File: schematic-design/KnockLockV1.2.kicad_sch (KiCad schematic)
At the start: 39 parts, among them IC1 ESP32-C3-WROOM-02-N4, IC2 LM2575-3.3WT, IC3 MC74HC74ADTR2G, J1 2477, J2 UJ20-C-H-G-TH-P16-TR, J3 TBP04R12-500-03BE, Q1 IRLML6402TRPBF, Q2 BC547B, U1 ADXL345BCCZ-RL7

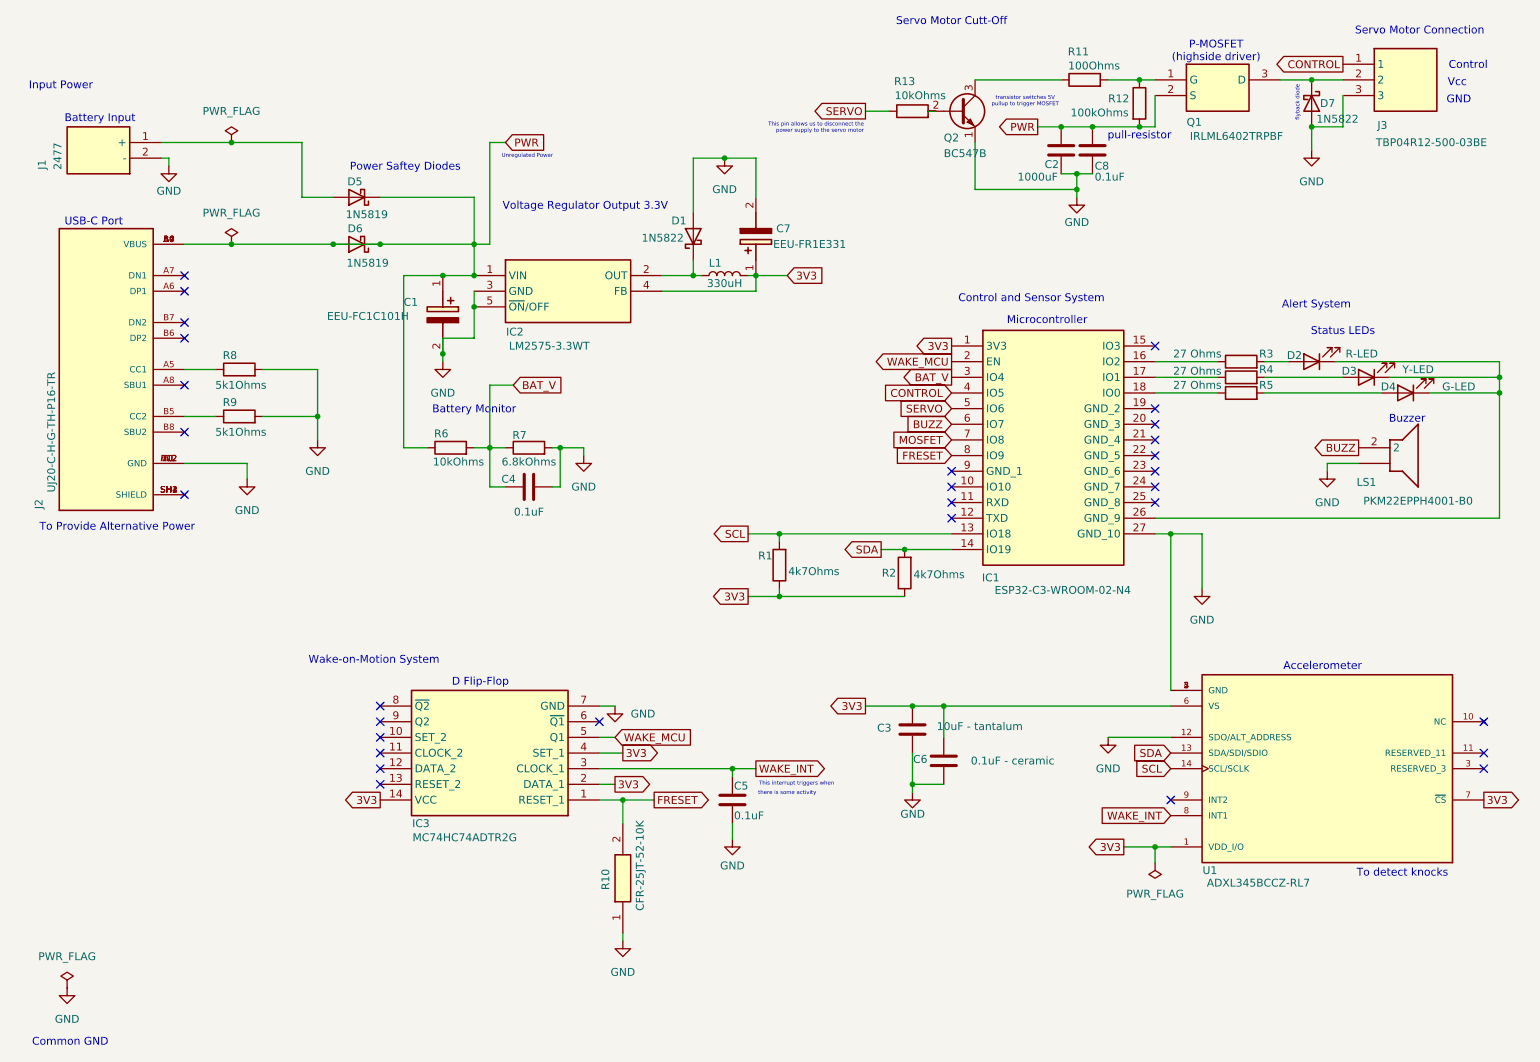
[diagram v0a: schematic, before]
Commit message: Fixed power gating
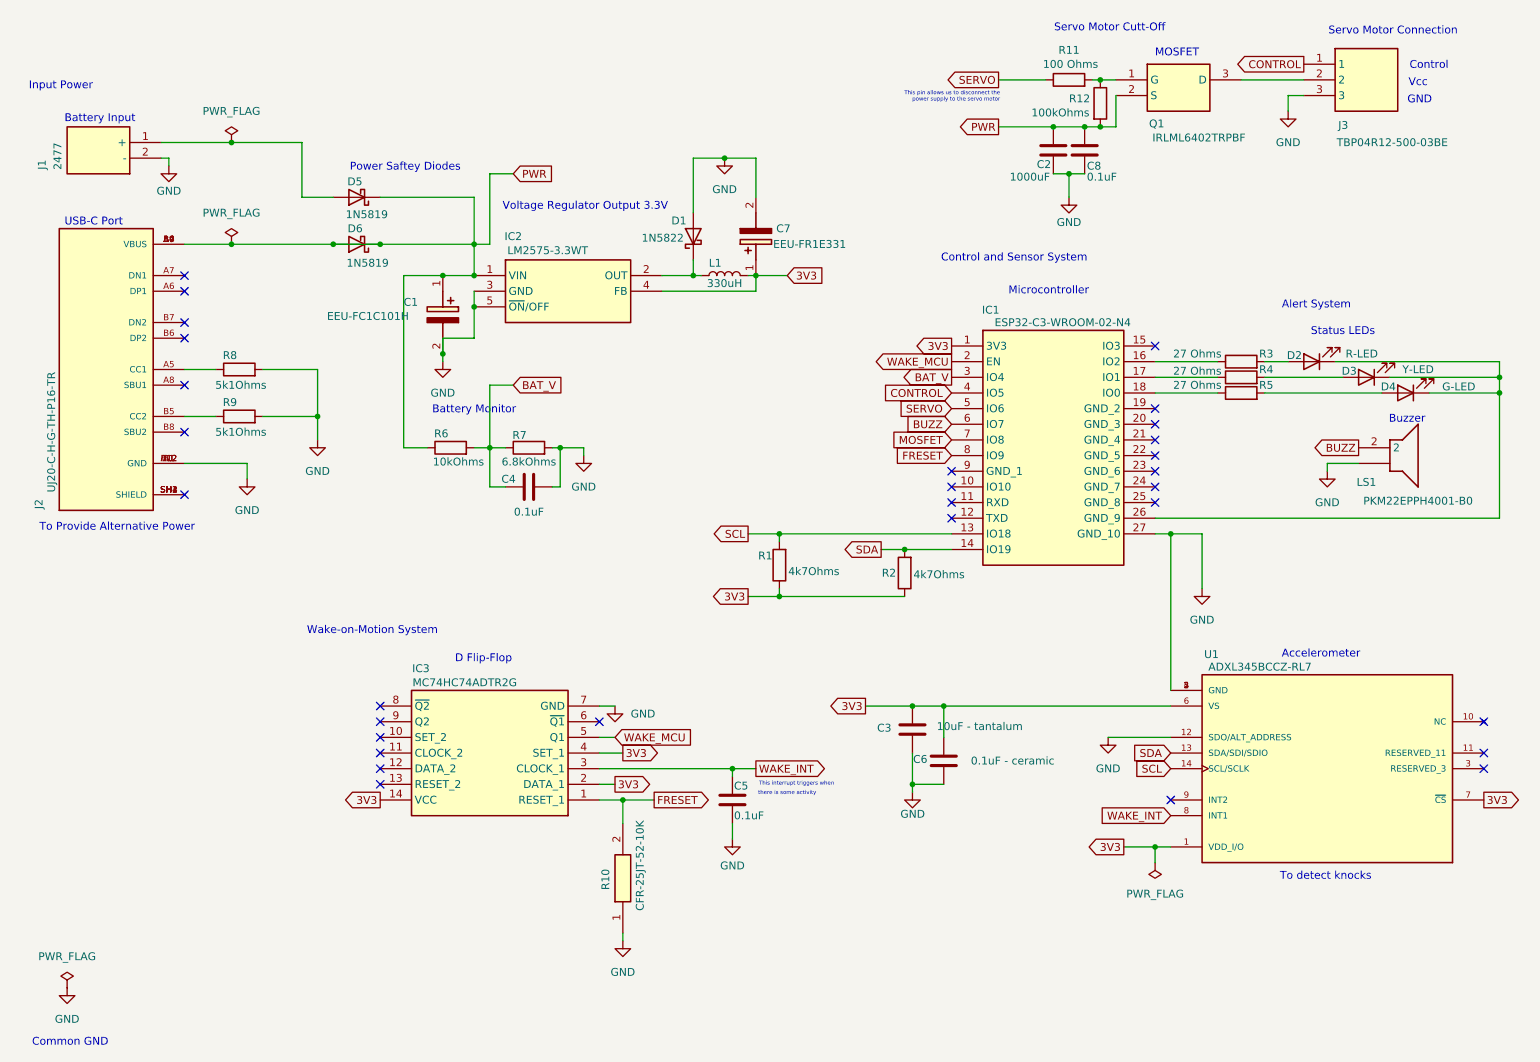
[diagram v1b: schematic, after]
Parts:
- removed D7: 1N5822, Diode_THT:D_DO-201AD_P15.24mm_Horizontal, symbol Diode:1N5822
- removed Q2: BC547B, Package_TO_SOT_THT:TO-92_HandSolder, symbol Transistor_BJT:2N3904
- removed R13: 10kOhms, symbol Device:R
- R11: value 100Ohms -> 100 Ohms
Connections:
- net SERVO: now also R11.1
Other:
- note added: "MOSFET"
- note removed: "P-MOSFET (highside driver)"
- note removed: "Unregulated Power"
- note removed: "flyback diode"
- note removed: "pull-resistor"
- note removed: "transistor switches 5V pullup to trigger MOSFET"
- moved on the sheet: C2, C8, J3, Q1, R11, R12
